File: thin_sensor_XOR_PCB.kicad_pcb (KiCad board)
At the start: 2 copper layers, 33 parts, among them U1 CD4030BM96

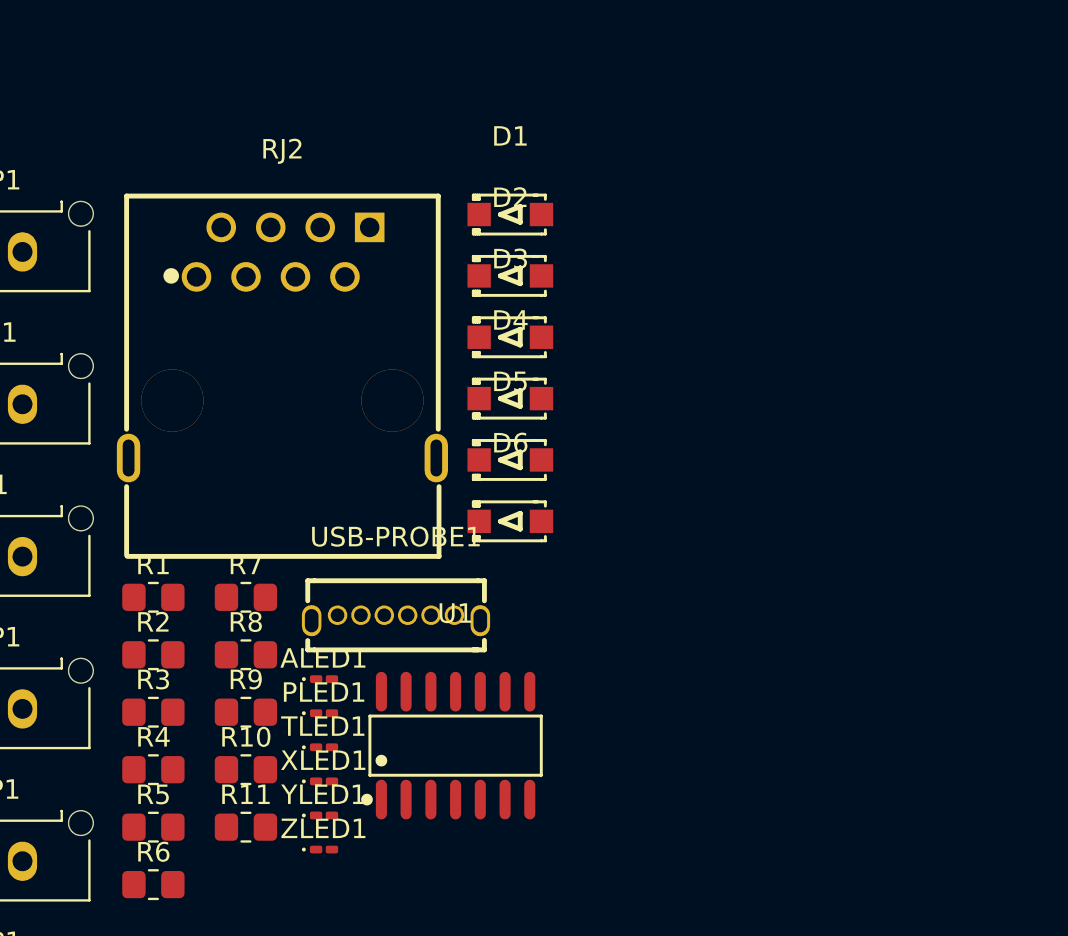
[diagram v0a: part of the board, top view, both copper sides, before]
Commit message: Removed the correct RJ45 port this time
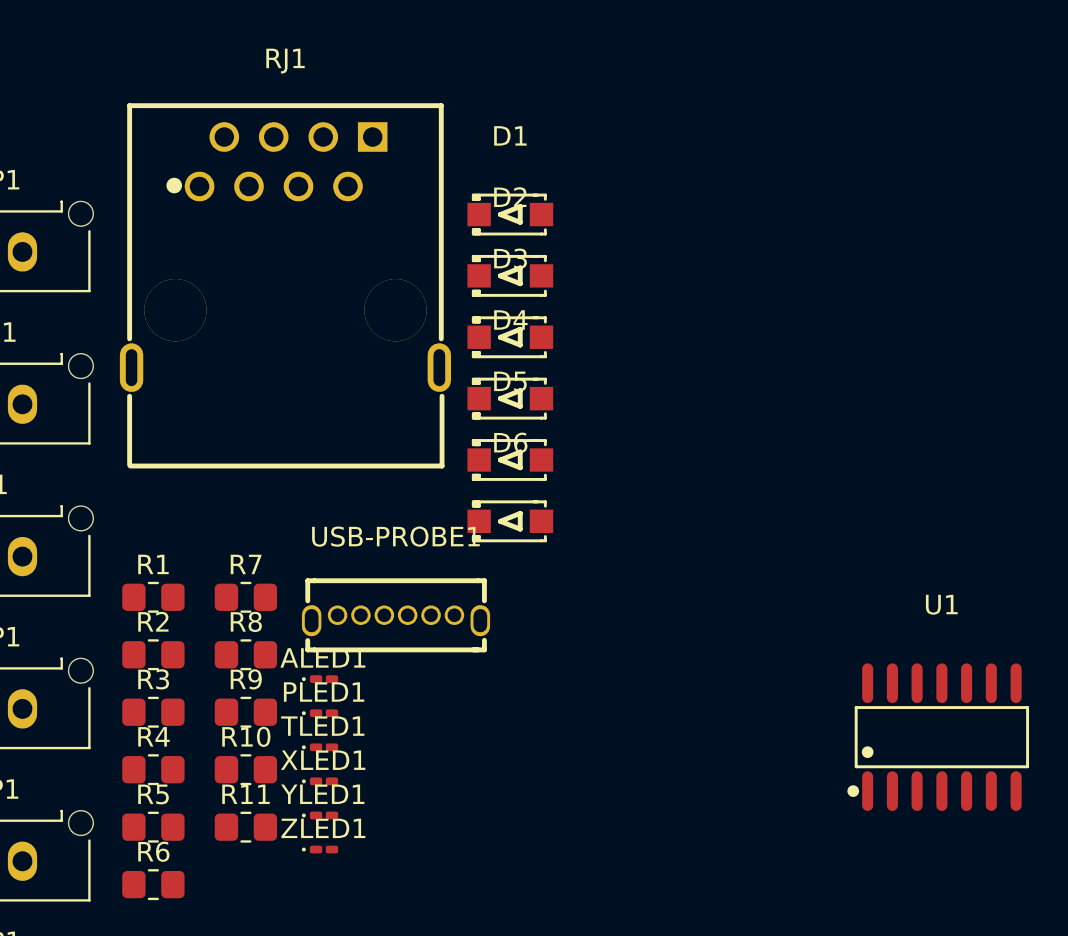
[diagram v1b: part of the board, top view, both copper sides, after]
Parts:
- removed RJ2: KH-RJ45-58-8P8C, thin sensor pcb custom:RJ45-TH_KH-RJ45-58-8P8C
- added RJ1: KH-RJ45-58-8P8C, thin sensor pcb custom:RJ45-TH_KH-RJ45-58-8P8C, F.Cu at (128.9, 71.5)
- moved U1 25.0 mm to (162.6, 96.4)
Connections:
- R1 pad 1: Xend2 -> Xend
- R2 pad 1: Yend2 -> Yend
- R3 pad 1: Zend2 -> Zend
- R7 pad 1: Xend1 -> Xend
- R8 pad 1: Yend1 -> Yend
- R9 pad 1: Zend1 -> Zend
- X-STOP1 pad 2: Xend2 -> Xend
- Y-STOP1 pad 2: Yend2 -> Yend
- Z-STOP1 pad 2: Zend2 -> Zend

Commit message: Finished schematic and layout
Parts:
- removed R10, R11, R8, R9: 33K, Resistor_SMD:R_0805_2012Metric_Pad1.20x1.40mm_HandSolder
- added EHALT1: Molex Microfit 3.0 436500215, thin sensor pcb custom:CONN-TH_436500215, F.Cu at (95.5, 127.0)
- added EHALTOUT1: Molex Microfit 3.0 436500215, thin sensor pcb custom:CONN-TH_436500215, F.Cu at (95.5, 136.0)
- added PROBEINV1: Header-Male-2.54_1x3, Connector_PinHeader_2.54mm:PinHeader_1x03_P2.54mm_Vertical, F.Cu at (104.9, 126.0)
- added REF**: MountingHole_3.2mm_M3, MountingHole:MountingHole_3.2mm_M3, F.Cu at (86.5, 70.0)
- added REF**: MountingHole_3.2mm_M3, MountingHole:MountingHole_3.2mm_M3, F.Cu at (113.5, 157.0)
- added TOOLOTINV1: Header-Male-2.54_1x3, Connector_PinHeader_2.54mm:PinHeader_1x03_P2.54mm_Vertical, F.Cu at (104.9, 138.0)
- A-STOP1, PROBE1, X-STOP1, Y-STOP1, Z-STOP1: footprint Connector_Molex:Molex_Micro-Fit_3.0_43650-0315_1x03_P3.00mm_Vertical -> thin sensor pcb custom:CONN-TH_436500315
- ALED1, PLED1: value SZYY0603B -> ~; footprint LED_SMD:LED_0201_0603Metric_Pad0.64x0.40mm_HandSolder -> thin sensor pcb custom:LED0805-RD_RED
- R7: footprint Resistor_SMD:R_0805_2012Metric_Pad1.20x1.40mm_HandSolder -> thin sensor pcb custom:R0805
- TLED1, YLED1: footprint LED_SMD:LED_0201_0603Metric_Pad0.64x0.40mm_HandSolder -> thin sensor pcb custom:LED0805-RD_RED
- TOOL1: value Molex Microfit 3.0 43650-0315 -> Molex Microfit 3.0 43650-0415; footprint Connector_Molex:Molex_Micro-Fit_3.0_43650-0315_1x03_P3.00mm_Vertical -> thin sensor pcb custom:CONN-TH_436500415
- U1: moved to B.Cu
- XLED1, ZLED1: value SZYY0603R -> ~; footprint LED_SMD:LED_0201_0603Metric_Pad0.64x0.40mm_HandSolder -> thin sensor pcb custom:LED0805-RD_RED
- moved RJ1 85.2 mm to (95.9, 150.1)
- moved USB-PROBE1 63.3 mm to (110.1, 148.6), turned to 90 degrees
- moved U1 54.7 mm to (108.2, 102.5), turned to -90 degrees
- moved R7 51.4 mm to (101.8, 134.0), turned to -90 degrees
- moved D5 49.7 mm to (106.0, 118.0), turned to -90 degrees
- moved D6 41.8 mm to (106.0, 109.0), turned to -90 degrees
- moved D4 40.3 mm to (106.0, 100.0), turned to -90 degrees
- moved D3 37.6 mm to (106.0, 91.0), turned to -90 degrees
- moved EHALTINV1 35.9 mm to (104.9, 132.0)
- moved D2 35.7 mm to (106.0, 82.0), turned to -90 degrees
- moved D1 34.6 mm to (106.0, 73.0), turned to -90 degrees
- moved TOOL1 33.0 mm to (95.5, 117.0)
- moved XLED1 32.2 mm to (111.4, 73.0), turned to -90 degrees
- moved PROBE1 31.8 mm to (96.0, 108.1)
- moved A-STOP1 30.7 mm to (96.0, 99.0)
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- renumbered T-----P-----G1 to EHALTINV1
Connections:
- net Probe2 renamed ProbeInput
- A-STOP1 pad 1: GND -> Net-(D4-K)
- A-STOP1 pad 3: Net-(D4-K) -> GND
- ALED1 pad 1: VCC -> Net-(ALED1-C)
- ALED1 pad 2: Net-(ALED1--) -> VCC
- EHALTINV1 pad 1: Tool -> VCC
- EHALTINV1 pad 2: Probe1 -> ExtEhaltInvert
- PLED1 pad 1: VCC -> Net-(PLED1-C)
- PLED1 pad 2: Net-(PLED1--) -> VCC
- PROBE1 pad 1: GND -> Net-(D6-K)
- PROBE1 pad 3: Net-(D6-K) -> GND
- R1 pad 2: Net-(XLED1--) -> Net-(XLED1-C)
- R2 pad 2: Net-(YLED1--) -> Net-(YLED1-C)
- R3 pad 2: Net-(ZLED1--) -> Net-(ZLED1-C)
- R4 pad 2: Net-(ALED1--) -> Net-(ALED1-C)
- R5 pad 2: Net-(TLED1--) -> Net-(TLED1-C)
- R6 pad 2: Net-(PLED1--) -> Net-(PLED1-C)
- R7 pad 1: Xend -> VCC
- R7 pad 2: VCC -> EhaltOut
- TLED1 pad 1: VCC -> Net-(TLED1-C)
- TLED1 pad 2: Net-(TLED1--) -> VCC
- TOOL1 pad 1: GND -> Net-(D5-K)
- TOOL1 pad 3: Net-(D5-K) -> ToolOvertravelInput
- U1 pad 1: unconnected-(U1-A-Pad1) -> ExtEhaltInput
- U1 pad 10: unconnected-(U1-L-Pad10) -> EhaltOut
- U1 pad 12: Probe1 -> ProbeInvert
- U1 pad 2: unconnected-(U1-B-Pad2) -> ExtEhaltInvert
- U1 pad 3: unconnected-(U1-J-Pad3) -> ExtEhalt
- U1 pad 4: unconnected-(U1-K-Pad4) -> ToolOvertravel
- U1 pad 5: unconnected-(U1-C-Pad5) -> ToolOvertravelInput
- U1 pad 6: unconnected-(U1-D-Pad6) -> ToolOverTravelInvert
- U1 pad 8: unconnected-(U1-E-Pad8) -> ExtEhalt
- U1 pad 9: unconnected-(U1-F-Pad9) -> ToolOvertravel
- X-STOP1 pad 1: GND -> Net-(D1-K)
- X-STOP1 pad 3: Net-(D1-K) -> GND
- XLED1 pad 1: VCC -> Net-(XLED1-C)
- XLED1 pad 2: Net-(XLED1--) -> VCC
- Y-STOP1 pad 1: GND -> Net-(D2-K)
- Y-STOP1 pad 3: Net-(D2-K) -> GND
- YLED1 pad 1: VCC -> Net-(YLED1-C)
- YLED1 pad 2: Net-(YLED1--) -> VCC
- Z-STOP1 pad 1: GND -> Net-(D3-K)
- Z-STOP1 pad 3: Net-(D3-K) -> GND
- ZLED1 pad 1: VCC -> Net-(ZLED1-C)
- ZLED1 pad 2: Net-(ZLED1--) -> VCC
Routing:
- net VCC: track 0.00 -> 150.9 mm, vias 0 -> 1
- net Xend: track 0.00 -> 104.1 mm
- net Yend: track 0.00 -> 100.4 mm, vias 0 -> 2
- net Zend: track 0.00 -> 94.4 mm, vias 0 -> 2
- net Aend: track 0.00 -> 87.2 mm, vias 0 -> 2
- net ProbeInput: track 0.00 -> 78.8 mm, vias 0 -> 2
- net Probe: track 0.00 -> 63.0 mm, vias 0 -> 7
- net ExtEhaltInput: track 0.00 -> 62.4 mm
- net Tool: track 0.00 -> 59.1 mm, vias 0 -> 2
- net EhaltOut: track 0.00 -> 56.7 mm, vias 0 -> 2
- net ToolOverTravelInvert: track 0.00 -> 44.2 mm
- net ExtEhaltInvert: track 0.00 -> 40.6 mm, vias 0 -> 2
- net Shield: track 0.00 -> 34.6 mm
- net ProbeInvert: track 0.00 -> 32.4 mm, vias 0 -> 2
- net ToolOvertravelInput: track 0.00 -> 24.9 mm
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- added copper zone on B.Cu, net GND
- added copper zone on F.Cu, net GND
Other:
- board outline added: 34 x 94 mm
